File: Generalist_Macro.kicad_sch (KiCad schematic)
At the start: 7 parts, among them SW1 SW_Push, SW2 SW_Push, SW3 SW_Push, SW4 SW_Push, U1 XIAO-RP2040-DIP

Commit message: Finished Schematic, Started PCB
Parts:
- removed D1, D2: SK6812MINI, LED_SMD:LED_SK6812MINI_PLCC4_3.5x3.5mm_P1.75mm, symbol LED:SK6812MINI
- removed SW4: SW_Push, Button_Switch_Keyboard:SW_Cherry_MX_1.00u_PCB, symbol Switch:SW_Push
- added D1, D2, D3, D4, D5, D6, D7, D8: 1N4148WT, Diode_SMD:D_SOD-523, symbol Diode:1N4148WT
- added D10, D11, D12, D13, D14, D15, D16, D17, D18, D19, D20, D21, D22, D23, D24, D9: WS2812B, LED_SMD:LED_WS2812B_PLCC4_5.0x5.0mm_P3.2mm, symbol LED:WS2812B
- added J1: OLED_DISPLAY, Connector_PinHeader_2.54mm:PinHeader_1x04_P2.54mm_Vertical, symbol Connector:Conn_01x04_Pin
- added SW13: RotaryEncoder_Switch, Rotary_Encoder:RotaryEncoder_Alps_EC11E-Switch_Vertical_H20mm, symbol Device:RotaryEncoder_Switch
- added SW5, SW6, SW7, SW8: SW_Push, Button_Switch_Keyboard:SW_Cherry_MX_1.00u_PCB, symbol Switch:SW_Push
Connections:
- net +5V: now also D10.1 (VDD), D11.1 (VDD), D12.1 (VDD), D13.1 (VDD), D14.1 (VDD), D15.1 (VDD), D16.1 (VDD), D17.1 (VDD), D18.1 (VDD), D19.1 (VDD), D20.1 (VDD), D21.1 (VDD), D22.1 (VDD), D23.1 (VDD), D9.1 (VDD), J1.3 (Pin_3)
- net GND: now also D10.3 (VSS), D11.3 (VSS), D12.3 (VSS), D13.3 (VSS), D14.3 (VSS), D15.3 (VSS), D16.3 (VSS), D17.3 (VSS), D18.3 (VSS), D19.3 (VSS), D20.3 (VSS), D21.3 (VSS), D22.3 (VSS), D23.3 (VSS), D24.3 (VSS), D9.3 (VSS), J1.4 (Pin_4), SW13.C; no longer SW1.1, SW2.1, SW3.1
- net at U1.5 (GPIO6/SDA): now also J1.1 (Pin_1)
- net at U1.11 (GPIO3/MOSI): now also U1.10 (GPIO4/MISO), SW13.A, SW13.B
- net at SW3.2: now also U1.3 (GPIO28/ADC2/A2), SW7.2; no longer U1.10 (GPIO4/MISO)
- net at SW1.2: now also U1.1 (GPIO26/ADC0/A0), SW5.2; no longer U1.8 (GPIO1/RX)
- net at U1.2 (GPIO27/ADC1/A1): now also SW2.2, SW6.2
- net at U1.4 (GPIO29/ADC3/A3): now also SW13.S1, SW8.2
- net at U1.6 (GPIO7/SCL): now also J1.2 (Pin_2)
- net at U1.7 (GPIO0/TX): now also D1.1 (K), D2.1 (K), D3.1 (K), D4.1 (K)
- net at U1.9 (GPIO2/SCK): now also D5.1 (K), D6.1 (K), D7.1 (K), D8.1 (K); no longer SW2.2
- new net: D5.2 (A), SW5.1
- new net: D20.2 (DOUT), D9.4 (DIN)
- new net: D20.4 (DIN), D21.2 (DOUT)
- new net: D15.2 (DOUT), D17.4 (DIN)
- new net: D14.2 (DOUT), D15.4 (DIN)
- new net: D13.2 (DOUT), D14.4 (DIN)
- new net: D3.2 (A), SW3.1
- new net: D10.4 (DIN), D9.2 (DOUT)
- new net: D21.4 (DIN), D23.2 (DOUT)
- new net: D1.2 (A), SW1.1
- new net: D2.2 (A), SW2.1
- new net: D10.2 (DOUT), D11.4 (DIN)
- new net: D12.2 (DOUT), D13.4 (DIN)
- new net: D11.2 (DOUT), D12.4 (DIN)
- new net: D6.2 (A), SW6.1
- new net: D19.2 (DOUT), D22.4 (DIN)
- new net: D18.2 (DOUT), D19.4 (DIN)
- new net: D16.4 (DIN), D22.2 (DOUT)
- new net: D23.4 (DIN), D24.2 (DOUT)
- new net: D16.2 (DOUT), D24.4 (DIN)
- new net: D8.2 (A), SW8.1
- new net: D4.2 (A), SW13.S2
- new net: D7.2 (A), SW7.1
- new net: D18.4 (DIN), U1.8 (GPIO1/RX)
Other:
- note added: "Column 1"
- note added: "Column 2"
- note added: "Column 3"
- note added: "Column 4"
- note added: "Key Matrix"
- note added: "Row 1"
- note added: "Row 2"
- moved on the sheet: SW1, U1

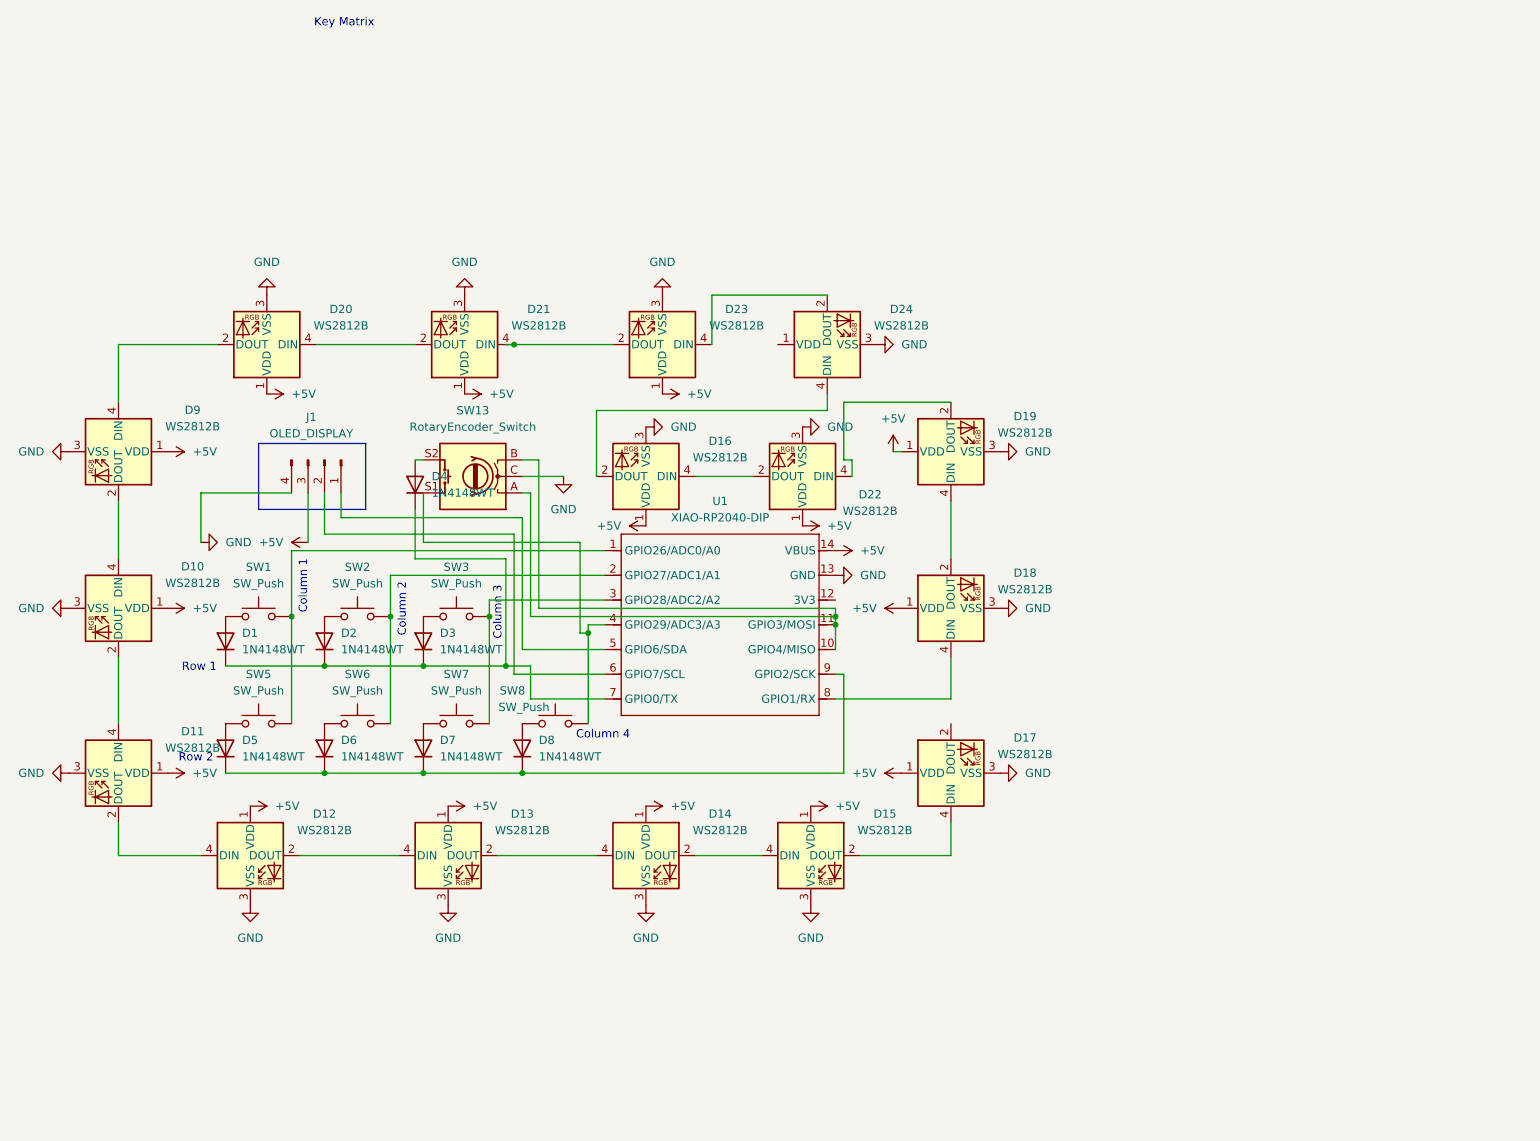
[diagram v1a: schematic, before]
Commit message: PCB laid out and wired. I just have to add the **Aesthetic** silkscreens now
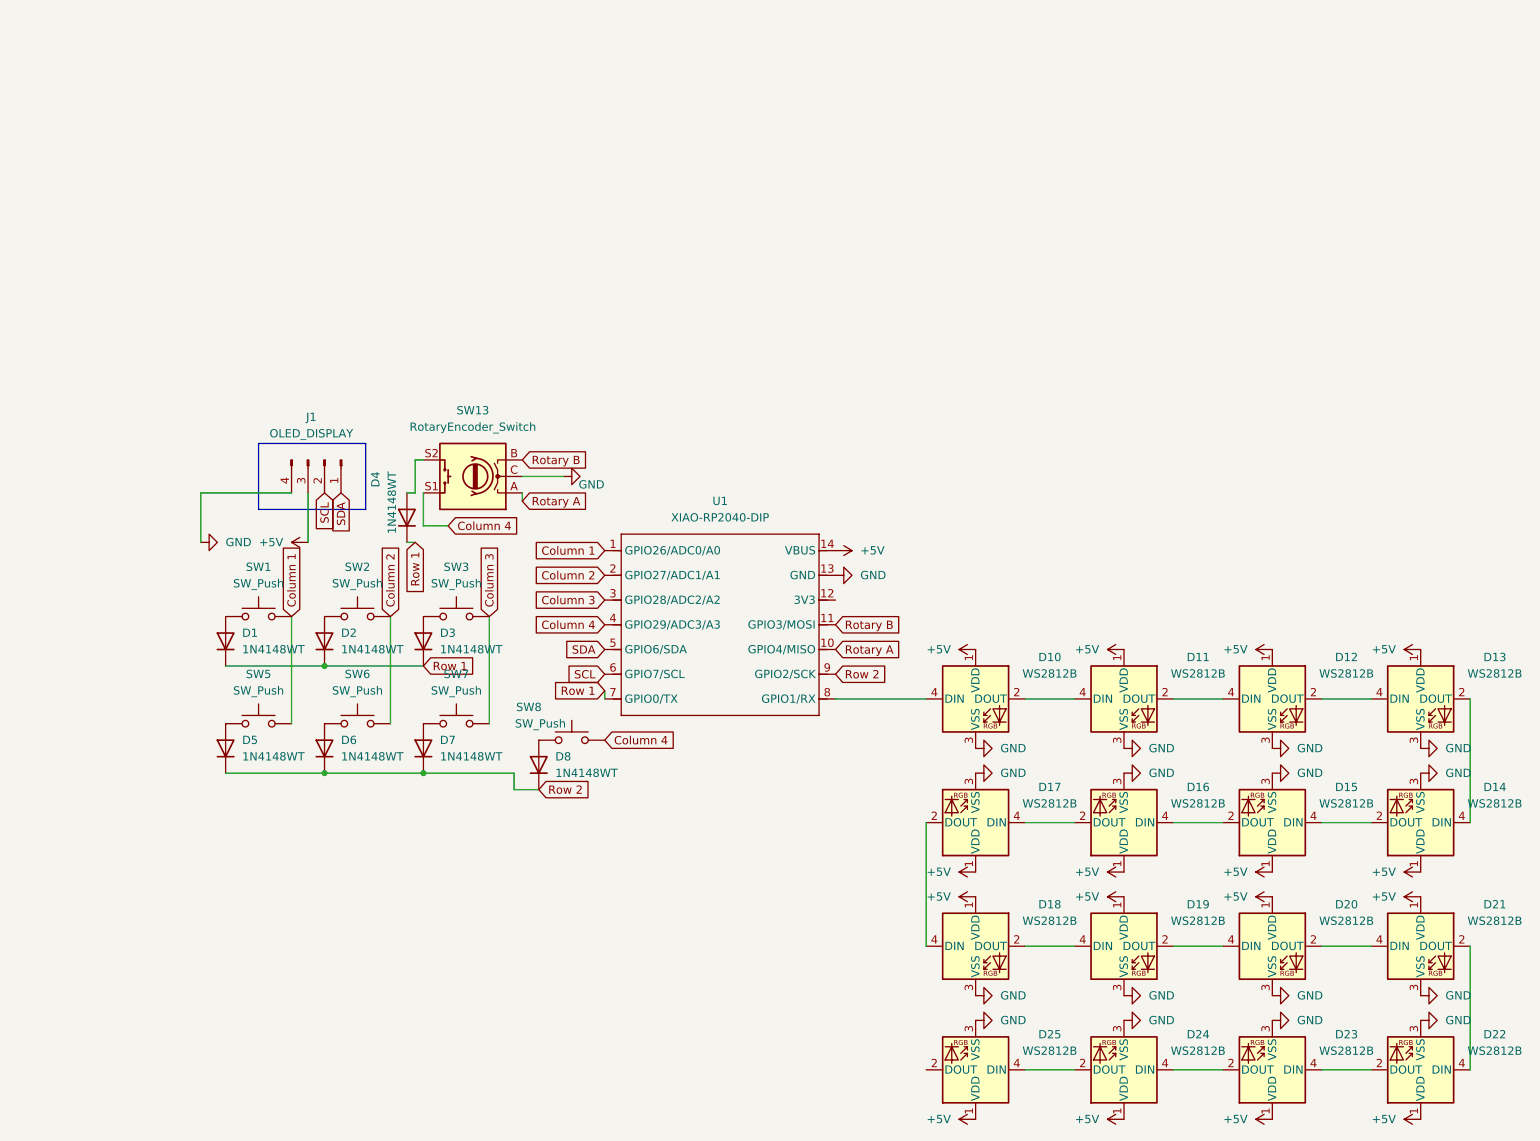
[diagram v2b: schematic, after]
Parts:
- removed D9: WS2812B, LED_SMD:LED_WS2812B_PLCC4_5.0x5.0mm_P3.2mm, symbol LED:WS2812B
- added D25: WS2812B, LED_SMD:LED_SK6812MINI_PLCC4_3.5x3.5mm_P1.75mm, symbol LED:WS2812B
- D10, D11, D12, D13, D14, D15, D16: footprint LED_SMD:LED_WS2812B_PLCC4_5.0x5.0mm_P3.2mm -> Backlight:MX_SK6812MINI-E_REV
- D17, D18, D19, D20, D21, D22, D23, D24: footprint LED_SMD:LED_WS2812B_PLCC4_5.0x5.0mm_P3.2mm -> LED_SMD:LED_SK6812MINI_PLCC4_3.5x3.5mm_P1.75mm
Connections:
- net +5V: now also D24.1 (VDD), D25.1 (VDD)
- net GND: now also D25.3 (VSS)
- net Column 1: now reaches SW1.2, SW5.2, U1.1 (GPIO26/ADC0/A0)
- net at D20.2 (DOUT): now also D21.4 (DIN)
- net at D21.2 (DOUT): now also D22.4 (DIN); no longer D20.4 (DIN)
- net Row 2: now reaches D5.1 (K), D6.1 (K), D7.1 (K), D8.1 (K), U1.9 (GPIO2/SCK)
- net at D17.4 (DIN): now also D16.2 (DOUT); no longer D15.2 (DOUT)
- net Row 1: now reaches D1.1 (K), D2.1 (K), D3.1 (K), D4.1 (K), U1.7 (GPIO0/TX)
- net at D17.2 (DOUT): now also D18.4 (DIN)
- net at D10.4 (DIN): now also U1.8 (GPIO1/RX)
- net at D23.2 (DOUT): now also D24.4 (DIN); no longer D21.4 (DIN)
- net Column 2: now reaches SW2.2, SW6.2, U1.2 (GPIO27/ADC1/A1)
- net Column 3: now reaches SW3.2, SW7.2, U1.3 (GPIO28/ADC2/A2)
- net at D19.2 (DOUT): now also D20.4 (DIN); no longer D22.4 (DIN)
- net at D22.2 (DOUT): now also D23.4 (DIN); no longer D16.4 (DIN)
- net at D24.2 (DOUT): now also D25.4 (DIN); no longer D23.4 (DIN)
- net SDA: now reaches J1.1 (Pin_1), U1.5 (GPIO6/SDA)
- net SCL: now reaches J1.2 (Pin_2), U1.6 (GPIO7/SCL)
- net Rotary A: now reaches SW13.A, U1.10 (GPIO4/MISO)
- net Rotary A: no longer SW13.B, U1.11 (GPIO3/MOSI)
- net Column 4: now reaches SW13.S1, SW8.2, U1.4 (GPIO29/ADC3/A3)
- new net: D15.2 (DOUT), D16.4 (DIN)
- new net Rotary B: SW13.B, U1.11 (GPIO3/MOSI)
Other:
- note removed: "Column 1"
- note removed: "Column 2"
- note removed: "Column 3"
- note removed: "Column 4"
- note removed: "Key Matrix"
- note removed: "Row 1"
- note removed: "Row 2"
- moved on the sheet: D4, D8, SW8
